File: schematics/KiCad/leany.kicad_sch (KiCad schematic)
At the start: 25 parts, among them J1 SWD, J2 SSD1306, SW1 BOOTMODE_SW, SW2 ZERO_BTN, SW3 HOLD_BTN, U1 LSM6DSO, U2 STM32F103C8Tx, U3 CH340C, Y1 8MHz

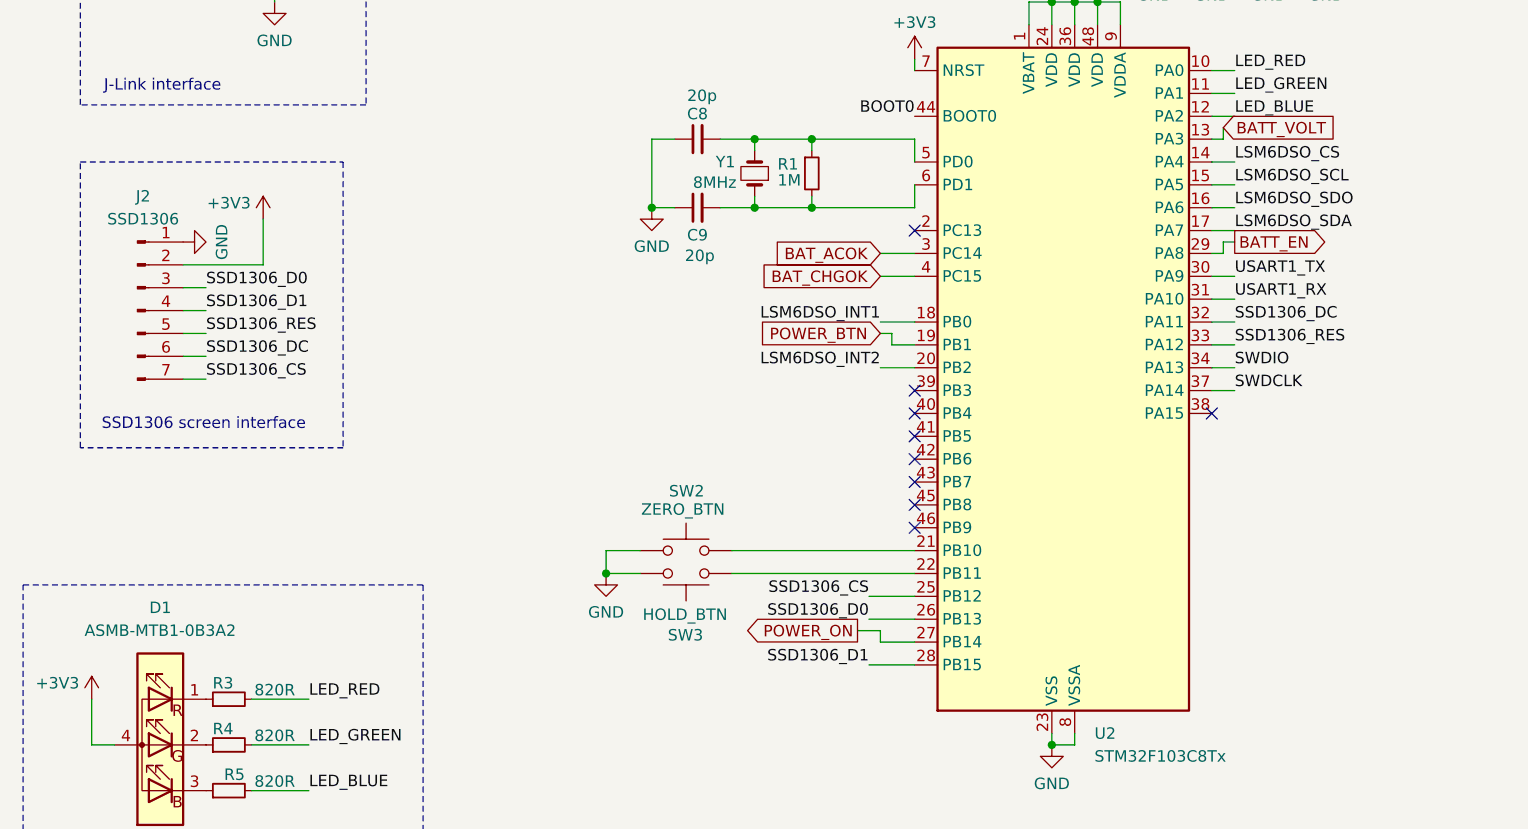
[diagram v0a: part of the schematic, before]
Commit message: replace connections in schematic
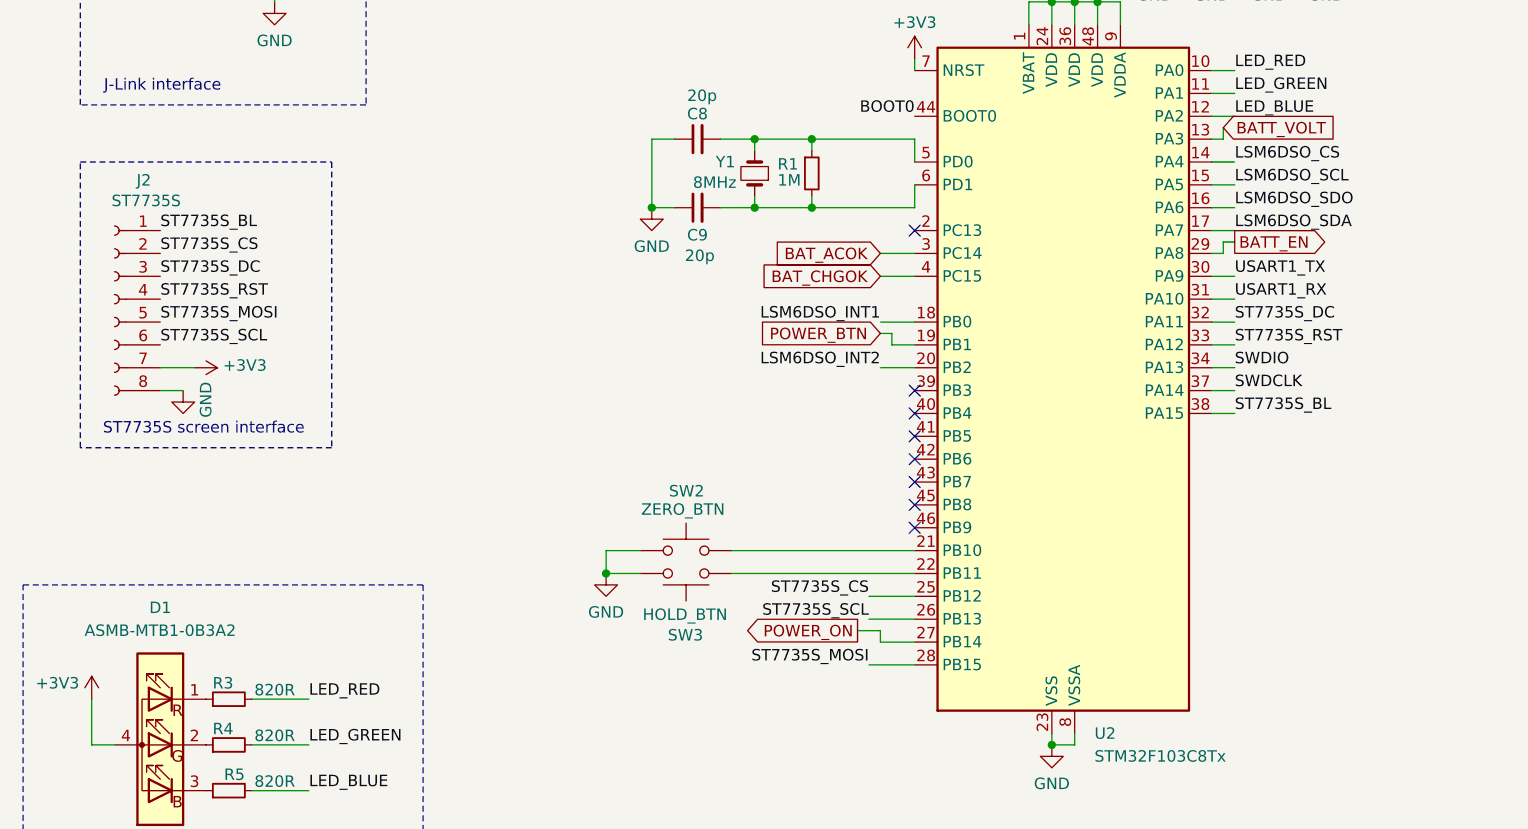
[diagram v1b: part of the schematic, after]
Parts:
- removed J2: SSD1306, Connector_PinHeader_1.00mm:PinHeader_1x07_P1.00mm_Vertical, symbol Connector:Conn_01x07_Pin
- added J2: ST7735S, Connector_PinSocket_1.00mm:PinSocket_1x08_P1.00mm_Vertical, symbol Connector:Conn_01x08_Socket
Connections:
- net +3V3: now also J2.7 (Pin_7)
- net GND: now also J2.8 (Pin_8)
- net ST7735S_BL: now reaches U2.38 (PA15)
- net ST7735S_BL: now also J2.1 (Pin_1)
- net SSD1306_CS renamed ST7735S_CS
- net ST7735S_CS: now also J2.2 (Pin_2)
- net SSD1306_D0 renamed ST7735S_SCL
- net ST7735S_SCL: now also J2.6 (Pin_6)
- net SSD1306_D1 renamed ST7735S_MOSI
- net ST7735S_MOSI: now also J2.5 (Pin_5)
- net SSD1306_DC renamed ST7735S_DC
- net ST7735S_DC: now also J2.3 (Pin_3)
- net SSD1306_RES renamed ST7735S_RST
- net ST7735S_RST: now also J2.4 (Pin_4)
- no-connect marks 16 -> 15
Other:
- note added: "ST7735S screen interface"
- note removed: "SSD1306 screen interface"

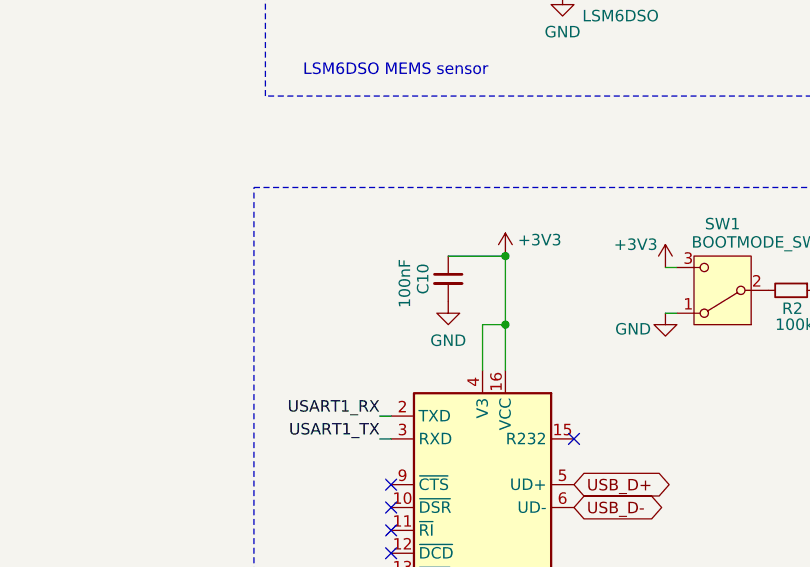
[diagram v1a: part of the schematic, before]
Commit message: assign capacitors footprints
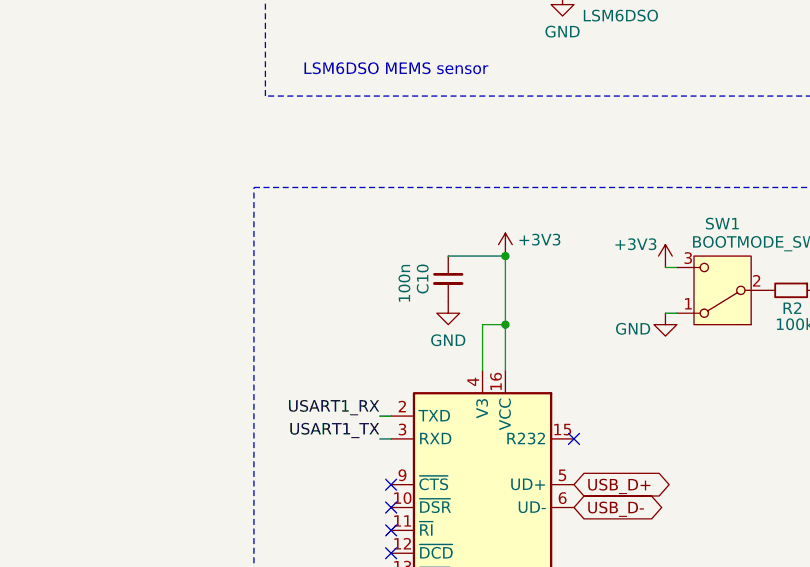
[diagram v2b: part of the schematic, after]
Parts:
- C1: footprint (none) -> Capacitor_SMD:C_0402_1005Metric
- C10: value 100nF -> 100n; footprint Capacitor_SMD:C_0201_0603Metric -> Capacitor_SMD:C_0402_1005Metric
- C2, C3, C4, C5, C6, C7: footprint Capacitor_SMD:C_0201_0603Metric -> Capacitor_SMD:C_0402_1005Metric
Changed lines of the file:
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@@
 	(title_block
 		(title "Leany")
-		(date "2024-09-08")
+		(date "2024-10-07")
 		(comment 1 "MIT License")
 		(comment 2 "Copyright (c) 2023 Gilles Henrard")
@@
 			)
 		)
-		(property "Footprint" "Capacitor_SMD:C_0201_0603Metric"
+		(property "Footprint" "Capacitor_SMD:C_0402_1005Metric"
 			(at 163.83 53.34 0)
 			(effects
@@
 			)
 		)
-		(property "Footprint" "Capacitor_SMD:C_0201_0603Metric"
+		(property "Footprint" "Capacitor_SMD:C_0402_1005Metric"
 			(at 46.99 54.61 0)
 			(effects
@@
 			)
 		)
-		(property "Footprint" "Capacitor_SMD:C_0201_0603Metric"
+		(property "Footprint" "Capacitor_SMD:C_0402_1005Metric"
 			(at 243.84 31.75 0)
 			(effects
@@
 			)
 		)
-		(property "Footprint" ""
+		(property "Footprint" "Capacitor_SMD:C_0402_1005Metric"
 			(at 238.76 31.75 0)
 			(effects
@@
 			)
 		)
-		(property "Footprint" "Capacitor_SMD:C_0201_0603Metric"
+		(property "Footprint" "Capacitor_SMD:C_0402_1005Metric"
 			(at 157.48 53.34 0)
 			(effects
@@
 			)
 		)
-		(property "Footprint" "Capacitor_SMD:C_0201_0603Metric"
+		(property "Footprint" "Capacitor_SMD:C_0402_1005Metric"
 			(at 144.78 53.34 0)
 			(effects
@@
 			)
 		)
-		(property "Footprint" "Capacitor_SMD:C_0201_0603Metric"
+		(property "Footprint" "Capacitor_SMD:C_0402_1005Metric"
 			(at 151.13 53.34 0)
 			(effects
@@
 			)
 		)
-		(property "Value" "100nF"
+		(property "Value" "100n"
 			(at 213.614 103.378 90)
 			(effects
@@
 			)
 		)
-		(property "Footprint" "Capacitor_SMD:C_0201_0603Metric"
+		(property "Footprint" "Capacitor_SMD:C_0402_1005Metric"
 			(at 218.44 102.87 0)
 			(effects

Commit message: fix misclicks
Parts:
- C8, C9: footprint Capacitor_SMD:C_0201_0603Metric -> Capacitor_SMD:C_0402_1005Metric
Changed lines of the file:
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@@
 			)
 		)
-		(property "Footprint" "Capacitor_SMD:C_0201_0603Metric"
+		(property "Footprint" "Capacitor_SMD:C_0402_1005Metric"
 			(at 93.98 83.82 0)
 			(effects
@@
 			)
 		)
-		(property "Footprint" "Capacitor_SMD:C_0201_0603Metric"
+		(property "Footprint" "Capacitor_SMD:C_0402_1005Metric"
 			(at 93.98 76.2 0)
 			(effects
